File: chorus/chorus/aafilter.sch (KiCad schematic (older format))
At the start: 7 parts, among them U6 TL072

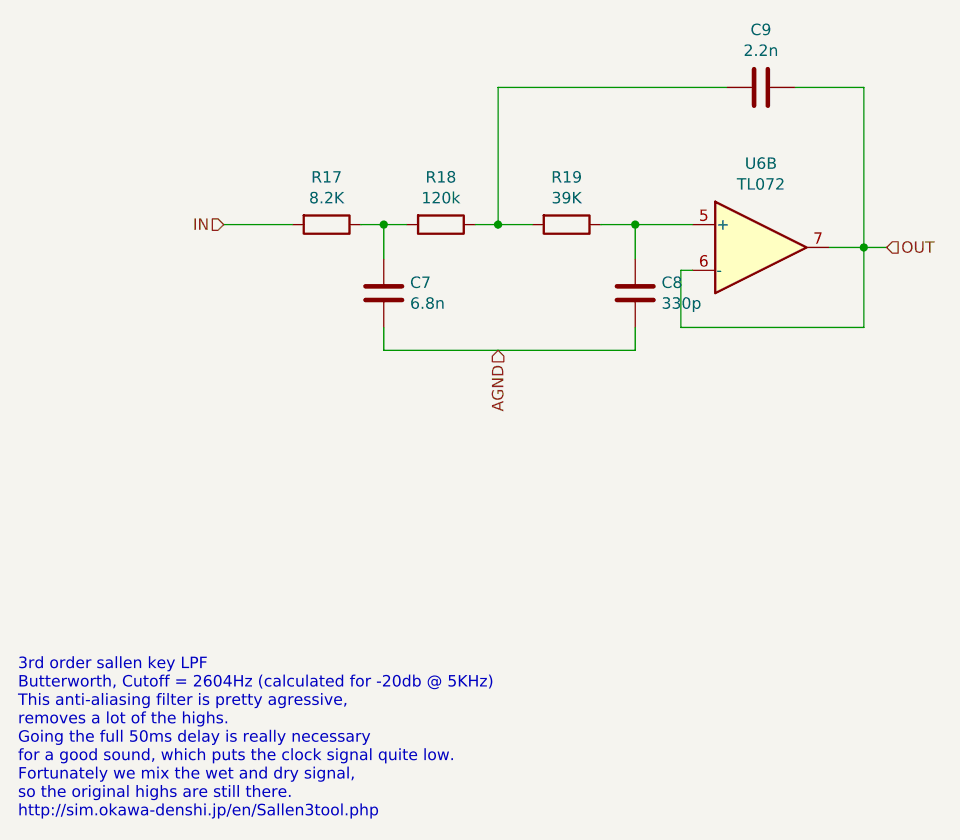
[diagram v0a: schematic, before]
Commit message: learnings from breadboard, attiny resolution is too low
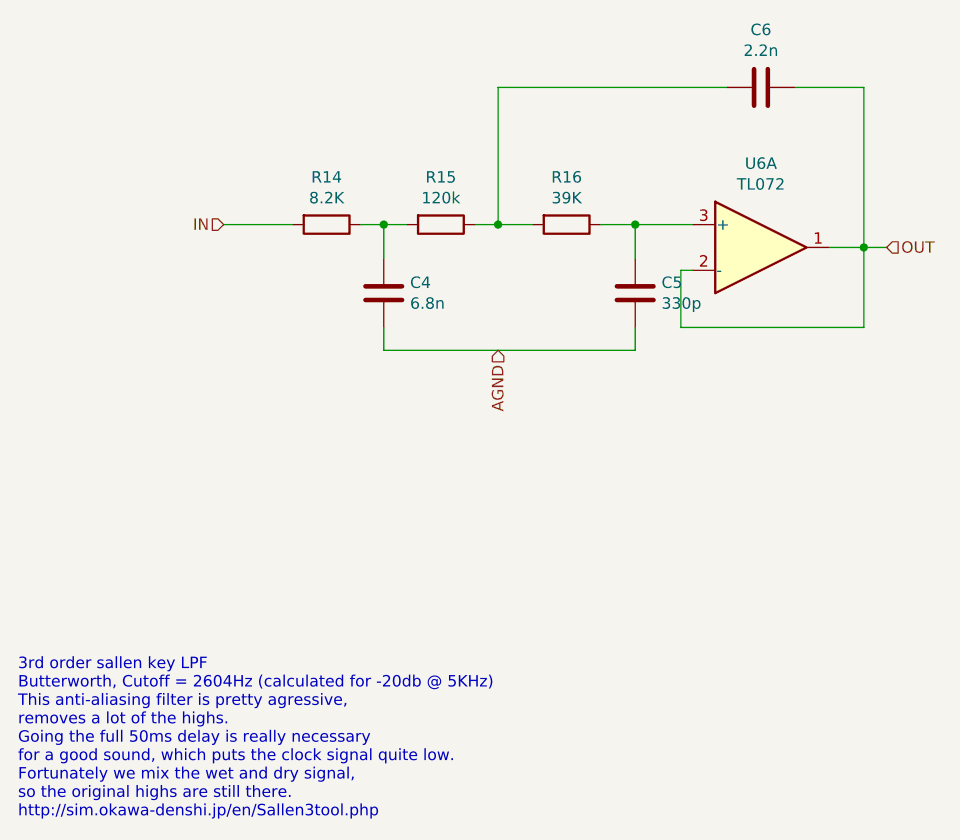
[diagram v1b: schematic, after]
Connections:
- net OUT: now also U6.1, U6.2 (-); no longer U6.6 (-), U6.7
- net at C5.2, R16.1: now also U6.3 (+); no longer U6.5 (+)
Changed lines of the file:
@@
 $Comp
 L Amplifier_Operational:TL072 U6
-U 2 1 62833F92
+U 1 1 62833F92
 P 5400 3800
 AR Path="/628336F3/62833F92" Ref="U6"  Part="1"
@@
 F 2 "Package_DIP:DIP-8_W7.62mm" H 5400 3800 50  0001 C CNN
 F 3 "http://www.ti.com/lit/ds/symlink/tl071.pdf" H 5400 3800 50  0001 C CNN
-	2    5400 3800
+	1    5400 3800
 	1    0    0    -1
 $EndComp
@@
 AR Path="/6287C7A2/62836D79" Ref="R?"  Part="1"
 AR Path="/629A6A5C/62836D79" Ref="R19"  Part="1"
-F 0 "R19" V 4343 3700 50  0000 C CNN
+F 0 "R16" V 4343 3700 50  0000 C CNN
 F 1 "39K" V 4434 3700 50  0000 C CNN
 F 2 "Resistor_THT:R_Axial_DIN0204_L3.6mm_D1.6mm_P2.54mm_Vertical" V 4480 3700 50  0001 C CNN
@@
 AR Path="/6287C7A2/62837E6B" Ref="R?"  Part="1"
 AR Path="/629A6A5C/62837E6B" Ref="R18"  Part="1"
-F 0 "R18" V 3793 3700 50  0000 C CNN
+F 0 "R15" V 3793 3700 50  0000 C CNN
 F 1 "120k" V 3884 3700 50  0000 C CNN
 F 2 "Resistor_THT:R_Axial_DIN0204_L3.6mm_D1.6mm_P2.54mm_Vertical" V 3930 3700 50  0001 C CNN
@@
 AR Path="/6287C7A2/62838612" Ref="R?"  Part="1"
 AR Path="/629A6A5C/62838612" Ref="R17"  Part="1"
-F 0 "R17" V 3293 3700 50  0000 C CNN
+F 0 "R14" V 3293 3700 50  0000 C CNN
 F 1 "8.2K" V 3384 3700 50  0000 C CNN
 F 2 "Resistor_THT:R_Axial_DIN0204_L3.6mm_D1.6mm_P2.54mm_Vertical" V 3430 3700 50  0001 C CNN
@@
 AR Path="/6287C7A2/62838D1A" Ref="C?"  Part="1"
 AR Path="/629A6A5C/62838D1A" Ref="C9"  Part="1"
-F 0 "C9" V 5148 3100 50  0000 C CNN
+F 0 "C6" V 5148 3100 50  0000 C CNN
 F 1 "2.2n" V 5239 3100 50  0000 C CNN
 F 2 "Capacitor_THT:C_Disc_D6.0mm_W2.5mm_P5.00mm" H 5438 2950 50  0001 C CNN
@@
 AR Path="/6287C7A2/62839637" Ref="C?"  Part="1"
 AR Path="/629A6A5C/62839637" Ref="C8"  Part="1"
-F 0 "C8" H 4735 3954 50  0000 R CNN
+F 0 "C5" H 4735 3954 50  0000 R CNN
 F 1 "330p" H 4735 4045 50  0000 R CNN
 F 2 "Capacitor_THT:C_Disc_D6.0mm_W2.5mm_P5.00mm" H 4888 3850 50  0001 C CNN
@@
 AR Path="/6287C7A2/62839D06" Ref="C?"  Part="1"
 AR Path="/629A6A5C/62839D06" Ref="C7"  Part="1"
-F 0 "C7" H 3635 3954 50  0000 R CNN
+F 0 "C4" H 3635 3954 50  0000 R CNN
 F 1 "6.8n" H 3635 4045 50  0000 R CNN
 F 2 "Capacitor_THT:C_Disc_D6.0mm_W2.5mm_P5.00mm" H 3788 3850 50  0001 C CNN

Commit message: redesign
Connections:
- net AGND renamed GNDA
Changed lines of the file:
@@
 $Descr A4 11693 8268
 encoding utf-8
-Sheet 2 3
+Sheet 2 6
 Title ""
 Date ""
@@
 	3750 4150 3750 4250
 Wire Wire Line
-	3750 4250 4850 4250
-Wire Wire Line
 	4850 4250 4850 4150
 Text HLabel 3050 3700 0    50   Input ~ 0
 IN
-Text HLabel 4250 4250 3    50   Input ~ 0
-AGND
 Text HLabel 5950 3800 2    50   Input ~ 0
 OUT
+$Comp
+L power:GNDA #PWR?
+U 1 1 630391FD
+P 3750 4250
+AR Path="/630391FD" Ref="#PWR?"  Part="1"
+AR Path="/628336F3/630391FD" Ref="#PWR0103"  Part="1"
+AR Path="/629A6A5C/630391FD" Ref="#PWR0110"  Part="1"
+F 0 "#PWR0103" H 3750 4000 50  0001 C CNN
+F 1 "GNDA" H 3755 4077 50  0000 C CNN
+F 2 "" H 3750 4250 50  0001 C CNN
+F 3 "" H 3750 4250 50  0001 C CNN
+	1    3750 4250
+	1    0    0    -1
+$EndComp
+$Comp
+L power:GNDA #PWR?
+U 1 1 630399DB
+P 4850 4250
+AR Path="/630399DB" Ref="#PWR?"  Part="1"
+AR Path="/628336F3/630399DB" Ref="#PWR0106"  Part="1"
+AR Path="/629A6A5C/630399DB" Ref="#PWR0112"  Part="1"
+F 0 "#PWR0106" H 4850 4000 50  0001 C CNN
+F 1 "GNDA" H 4855 4077 50  0000 C CNN
+F 2 "" H 4850 4250 50  0001 C CNN
+F 3 "" H 4850 4250 50  0001 C CNN
+	1    4850 4250
+	1    0    0    -1
+$EndComp
 $EndSCHEMATC

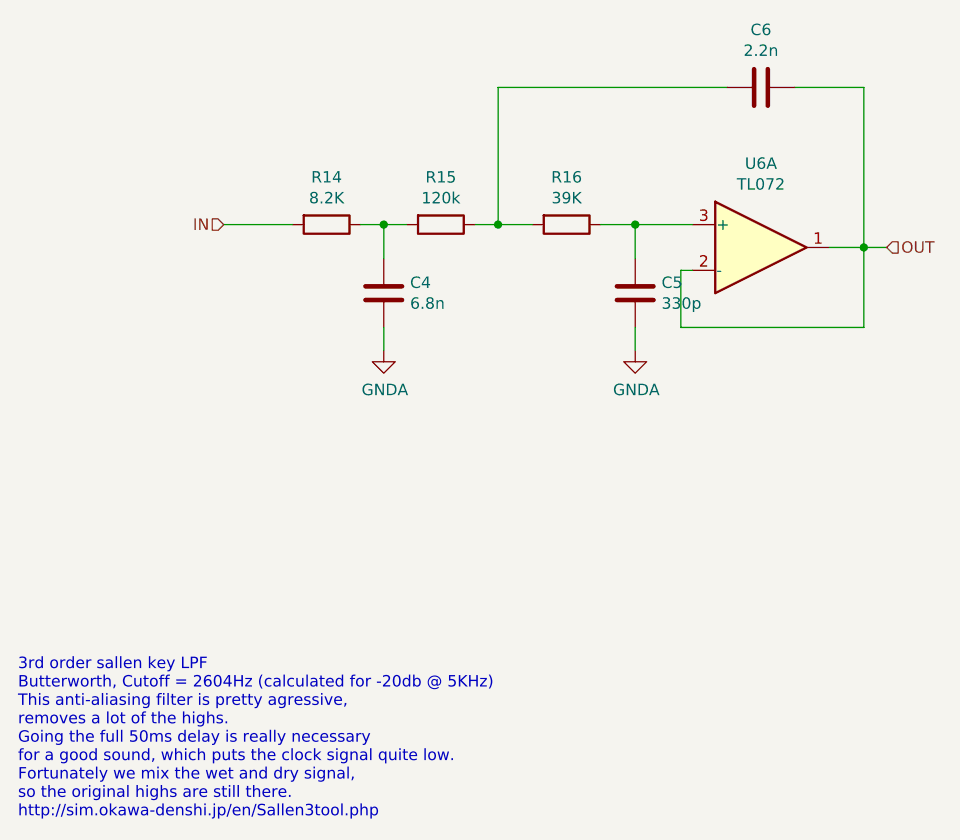
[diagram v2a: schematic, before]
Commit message: add wet/dry mix and recalculate filters
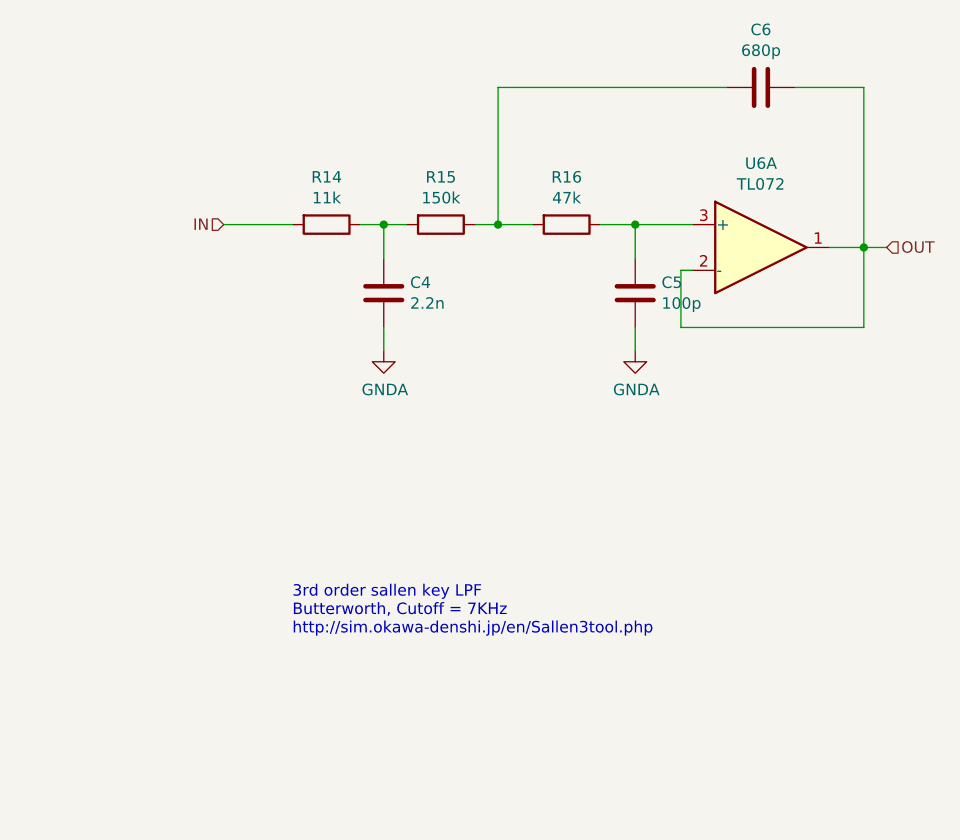
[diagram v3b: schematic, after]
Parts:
- C4: value 6.8n -> 2.2n
- C5: value 330p -> 100p
- C6: value 2.2n -> 680p
- R14: value 8.2K -> 11k
- R15: value 120k -> 150k
- R16: value 39K -> 47k
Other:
- note added: "3rd order sallen key LPF\nButterworth, Cutoff = 7KHz\nhttp://sim.okawa-denshi.jp/en/Sallen3tool.php"
- note removed: "3rd order sallen key LPF\nButterworth, Cutoff = 2604Hz (calculated for -20db @ 5KHz)\nThis anti-aliasing filter is pretty agressive,\nremoves a lot of the highs.\nGoing the full 50ms delay is really necessary\nfor a good sound, which puts the clock signal quite low.\nFortunately we mix the wet and dry signal,\nso the original highs are still there.\nhttp://sim.okawa-denshi.jp/en/Sallen3tool.php"
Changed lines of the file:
@@
 AR Path="/629A6A5C/62836D79" Ref="R19"  Part="1"
 F 0 "R16" V 4343 3700 50  0000 C CNN
-F 1 "39K" V 4434 3700 50  0000 C CNN
+F 1 "47k" V 4434 3700 50  0000 C CNN
 F 2 "Resistor_THT:R_Axial_DIN0204_L3.6mm_D1.6mm_P2.54mm_Vertical" V 4480 3700 50  0001 C CNN
 F 3 "~" H 4550 3700 50  0001 C CNN
@@
 AR Path="/629A6A5C/62837E6B" Ref="R18"  Part="1"
 F 0 "R15" V 3793 3700 50  0000 C CNN
-F 1 "120k" V 3884 3700 50  0000 C CNN
+F 1 "150k" V 3884 3700 50  0000 C CNN
 F 2 "Resistor_THT:R_Axial_DIN0204_L3.6mm_D1.6mm_P2.54mm_Vertical" V 3930 3700 50  0001 C CNN
 F 3 "~" H 4000 3700 50  0001 C CNN
@@
 AR Path="/629A6A5C/62838612" Ref="R17"  Part="1"
 F 0 "R14" V 3293 3700 50  0000 C CNN
-F 1 "8.2K" V 3384 3700 50  0000 C CNN
+F 1 "11k" V 3384 3700 50  0000 C CNN
 F 2 "Resistor_THT:R_Axial_DIN0204_L3.6mm_D1.6mm_P2.54mm_Vertical" V 3430 3700 50  0001 C CNN
 F 3 "~" H 3500 3700 50  0001 C CNN
@@
 	0    1    1    0
 $EndComp
-Text Notes 2150 6300 0    50   ~ 0
-3rd order sallen key LPF\nButterworth, Cutoff = 2604Hz (calculated for -20db @ 5KHz)\nThis anti-aliasing filter is pretty agressive,\nremoves a lot of the highs.\nGoing the full 50ms delay is really necessary\nfor a good sound, which puts the clock signal quite low.\nFortunately we mix the wet and dry signal,\nso the original highs are still there.\nhttp://sim.okawa-denshi.jp/en/Sallen3tool.php
+Text Notes 3350 5500 0    50   ~ 0
+3rd order sallen key LPF\nButterworth, Cutoff = 7KHz\nhttp://sim.okawa-denshi.jp/en/Sallen3tool.php
 $Comp
 L Device:C C6
@@
 AR Path="/629A6A5C/62838D1A" Ref="C9"  Part="1"
 F 0 "C6" V 5148 3100 50  0000 C CNN
-F 1 "2.2n" V 5239 3100 50  0000 C CNN
+F 1 "680p" V 5239 3100 50  0000 C CNN
 F 2 "Capacitor_THT:C_Disc_D6.0mm_W2.5mm_P5.00mm" H 5438 2950 50  0001 C CNN
 F 3 "~" H 5400 3100 50  0001 C CNN
@@
 AR Path="/629A6A5C/62839637" Ref="C8"  Part="1"
 F 0 "C5" H 4735 3954 50  0000 R CNN
-F 1 "330p" H 4735 4045 50  0000 R CNN
+F 1 "100p" H 4735 4045 50  0000 R CNN
 F 2 "Capacitor_THT:C_Disc_D6.0mm_W2.5mm_P5.00mm" H 4888 3850 50  0001 C CNN
 F 3 "~" H 4850 4000 50  0001 C CNN
@@
 AR Path="/629A6A5C/62839D06" Ref="C7"  Part="1"
 F 0 "C4" H 3635 3954 50  0000 R CNN
-F 1 "6.8n" H 3635 4045 50  0000 R CNN
+F 1 "2.2n" H 3635 4045 50  0000 R CNN
 F 2 "Capacitor_THT:C_Disc_D6.0mm_W2.5mm_P5.00mm" H 3788 3850 50  0001 C CNN
 F 3 "~" H 3750 4000 50  0001 C CNN
